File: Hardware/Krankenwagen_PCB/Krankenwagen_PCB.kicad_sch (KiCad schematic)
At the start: 12 parts, among them J1 XT60-M, J2 XT60-M, J3 XT60-M

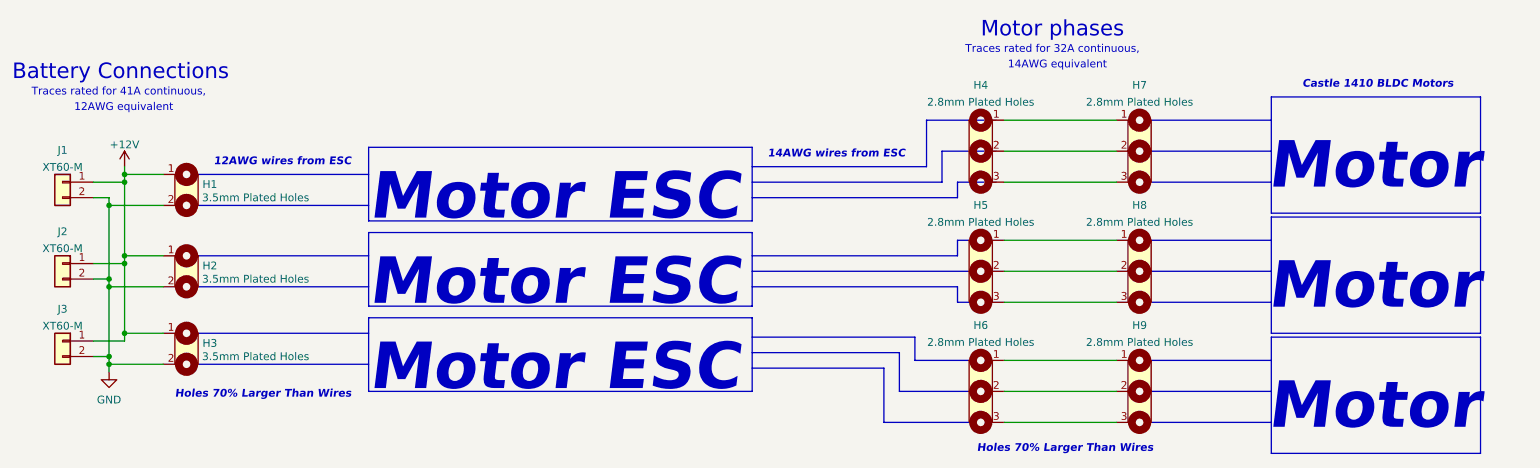
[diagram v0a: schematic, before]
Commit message: Basic PCB completed, added logos to silkscreen
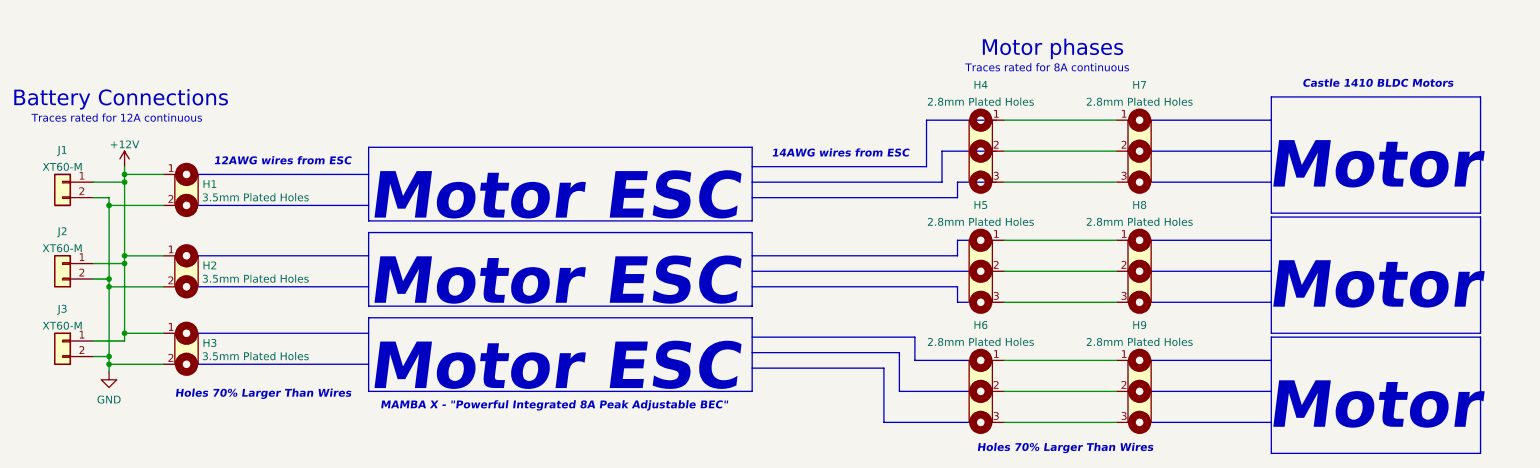
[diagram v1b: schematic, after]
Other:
- note added: "MAMBA X - "Powerful Integrated 8A Peak Adjustable BEC""
- note added: "Traces rated for 12A continuous"
- note added: "Traces rated for 8A continuous"
- note removed: "12AWG equivalent"
- note removed: "14AWG equivalent"
- note removed: "Traces rated for 32A continuous,"
- note removed: "Traces rated for 41A continuous,"
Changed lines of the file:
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@@
     (stroke (width 0) (type default) (color 0 0 0 0))
   )
-  (text "Battery Connections" (at 33.02 59.69 0)
+  (text "Battery Connections" (at 33.02 64.135 0)
     (effects (font (size 2.54 2.54)) (justify left bottom))
   )
@@
     (effects (font (size 7.62 7.62) (thickness 1.524) bold italic) (justify left bottom))
   )
-  (text "Motor phases" (at 191.77 52.705 0)
+  (text "Motor phases" (at 191.77 55.88 0)
     (effects (font (size 2.54 2.54)) (justify left bottom))
   )
@@
     (effects (font (size 7.62 7.62) (thickness 1.524) bold italic) (justify left bottom))
   )
+  (text "MAMBA X - \"Powerful Integrated 8A Peak Adjustable BEC\""
+    (at 93.345 113.665 0)
+    (effects (font (size 1.27 1.27) bold italic) (justify left bottom))
+  )
   (text "Motor" (at 238.76 78.105 0)
     (effects (font (size 7.62 7.62) (thickness 1.524) bold italic) (justify left bottom))
-  )
-  (text "14AWG wires from ESC" (at 156.845 72.39 0)
-    (effects (font (size 1.27 1.27) bold italic) (justify left bottom))
   )
   (text "Motor ESC" (at 91.44 97.155 0)
     (effects (font (size 7.62 7.62) (thickness 1.524) bold italic) (justify left bottom))
   )
-  (text "12AWG equivalent" (at 43.18 64.77 0)
+  (text "Traces rated for 12A continuous" (at 36.195 66.675 0)
     (effects (font (size 1.27 1.27)) (justify left bottom))
   )
-  (text "Traces rated for 41A continuous," (at 36.195 62.23 0)
-    (effects (font (size 1.27 1.27)) (justify left bottom))
-  )
-  (text "Traces rated for 32A continuous," (at 189.23 55.245 0)
-    (effects (font (size 1.27 1.27)) (justify left bottom))
-  )
-  (text "14AWG equivalent" (at 196.215 57.785 0)
+  (text "Traces rated for 8A continuous" (at 189.23 58.42 0)
     (effects (font (size 1.27 1.27)) (justify left bottom))
   )
@@
     (effects (font (size 7.62 7.62) (thickness 1.524) bold italic) (justify left bottom))
   )
+  (text "14AWG wires from ESC" (at 157.48 72.39 0)
+    (effects (font (size 1.27 1.27) bold italic) (justify left bottom))
+  )
   (symbol (lib_name "MountingHole_3") (lib_id "Mechanical:MountingHole") (at 61.595 100.965 0) (unit 1)
